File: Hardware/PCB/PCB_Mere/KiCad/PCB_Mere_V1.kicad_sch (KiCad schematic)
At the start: 24 parts, among them U1 STM32H723ZGTx, U2 SX1276

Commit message: Add files via upload
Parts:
- removed U1: STM32H723ZGTx, Package_QFP:LQFP-144_20x20mm_P0.5mm, symbol MCU_ST_STM32H7:STM32H723ZGTx
- removed U2: SX1276, Package_DFN_QFN:QFN-28-1EP_6x6mm_P0.65mm_EP4.8x4.8mm, symbol RF:SX1276
- added U1: STM32H723ZGT6, EasyEDA:LQFP-144_L20.0-W20.0-P0.50-LS22.0-BL, symbol EasyEDA:STM32H723ZGT6
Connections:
- net +3.3V: now also C2.1, U1.107 (VSS), U1.108 (VDD), U1.120 (VSS), U1.121 (VDD), U1.130 (VSS), U1.131 (VDD), U1.143 (PDR_ON), U1.144 (VDD), U1.16 (VSS), U1.17 (VDD), U1.30 (VDD), U1.31 (VSSA), U1.32 (VREF+), U1.33 (VDDA), U1.38 (VSS), U1.39 (VDD), U1.51 (VSS), U1.52 (VDD), U1.6 (VBAT), U1.61 (VSS), U1.62 (VDD), U1.72 (VDD), U1.83 (VSS), U1.84 (VDD), U1.94 (VSS), U1.95 (VDD33USB); no longer C2.2
- net DEBUG_JTCK-SWCLK: now also U1.109 (PA14)
- net DEBUG_JTDO-SWO: now also U1.133 (PB3)
- net DEBUG_JTMS-SWDIO: now also U1.105 (PA13)
- net ESP32_UART7_RX: now also U1.58 (PE7)
- net ESP32_UART7_TX: now also U1.59 (PE8)
- net ETAT-B-ON/OFF_GPIO_Input: now also U1.29 (PC3_C)
- net GNSS_UART5_RX: now also U1.73 (PB12)
- net GNSS_UART5_TX: now also U1.74 (PB13)
- net ID-EXT_ADC1_INP14: now also U1.36 (PA2)
- net IMU-F_I2C2_SCL: now also U1.11 (PF1)
- net IMU-F_I2C2_SDA: now also U1.10 (PF0)
- net IMU-M_I2C1_SCL: now also U1.136 (PB6)
- net IMU-M_I2C1_SDA: now also U1.137 (PB7)
- net JOYSTICK_ADC1_INP10: now also U1.26 (PC0)
- net JOYSTICK_ADC1_INP11: now also U1.27 (PC1)
- net JOYSTICK_GPIO_Input: now also U1.28 (PC2_C)
- net JTAG_UART9_RX: now also U1.56 (PG0)
- net JTAG_UART9_TX: now also U1.57 (PG1)
- net LED1_ETAT_GPIO_Output: now also U1.81 (PD12)
- net LED2_DEBUG_GPIO_Output: now also U1.80 (PD11)
- net LIDAR_UART8_RX: now also U1.141 (PE0)
- net LIDAR_UART8_TX: now also U1.142 (PE1)
- net LoRa_SPI1_MISO: now also U1.124 (PG9)
- net LoRa_SPI1_MOSI: now also U1.123 (PD7)
- net LoRa_SPI1_NSS: now also U1.125 (PG10)
- net LoRa_SPI1_SCK: now also U1.126 (PG11)
- net SCREEN_SPI5_MISO: now also U1.20 (PF8)
- net SCREEN_SPI5_MOSI: now also U1.21 (PF9)
- net SCREEN_SPI5_NSS: now also U1.18 (PF6)
- net SCREEN_SPI5_SCK: now also U1.19 (PF7)
- net SD_CK: now also U1.113 (PC12)
- net SD_CMD: now also U1.116 (PD2)
- net SD_D0: now also U1.98 (PC8)
- net SD_D1: now also U1.99 (PC9)
- net SD_D2: now also U1.111 (PC10)
- net SD_D3: now also U1.112 (PC11)
- net SD_DETECT: now also U1.97 (PC7)
- net STEPPER-AZ_TIM8_CH1: now also U1.96 (PC6)
- net STEPPER-EL_TIM1_CH1: now also U1.60 (PE9)
- net TMC2209_AZ_DIAG_GPIO_Input: now also U1.87 (PG2)
- net TMC2209_AZ_DIR_GPIO_Output: now also U1.90 (PG5)
- net TMC2209_AZ_ENABLE_GPIO_Output: now also U1.92 (PG7)
- net TMC2209_AZ_INDEX_GPIO_Input: now also U1.86 (PD15)
- net TMC2209_AZ_MS1_GPIO_Output: now also U1.89 (PG4)
- net TMC2209_AZ_MS2_GPIO_Output: now also U1.88 (PG3)
- net TMC2209_AZ_STEP_GPIO_Output: now also U1.91 (PG6)
- net TMC2209_AZ_USART1_RX: now also U1.76 (PB15)
- net TMC2209_AZ_USART1_TX: now also U1.75 (PB14)
- net TMC2209_EL_DIAG_GPIO_Input: now also U1.68 (PE15)
- net TMC2209_EL_DIR_GPIO_Output: now also U1.65 (PE12)
- net TMC2209_EL_ENABLE_GPIO_Output: now also U1.63 (PE10)
- net TMC2209_EL_INDEX_GPIO_Input: now also U1.69 (PB10)
- net TMC2209_EL_MS1_GPIO_Output: now also U1.66 (PE13)
- net TMC2209_EL_MS2_GPIO_Output: now also U1.67 (PE14)
- net TMC2209_EL_STEP_GPIO_Output: now also U1.64 (PE11)
- net TMC2209_EL_USART3_RX: now also U1.70 (PB11)
- net TMC2209_EL_USART3_TX: now also U1.77 (PD8)
- net at C7.2: now also U1.25 (NRST)
- net at R1.2: now also U1.138 (BOOT0)
- net at C3.1: now also U1.106 (VCAP)
- new net: C2.2, U1.71 (VCAP)
- new net SCREEN_RST_GPIO_Output: U1.22 (PF10)
- no-connect marks 57 -> 56
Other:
- added sheet Composant_Mère (Composant_Mere.kicad_sch)
- added sheet Connecteurs -> PCB (Connecteurs.kicad_sch)
- note added: "STM32H723ZGTx"
- note removed: "STM32H723ZGTx Main PCB Mère"
- moved on the sheet: C1, C10, C11, C12, C13, C14, C15, C16, C17, C18, C19, C2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

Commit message: push du kicad
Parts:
- removed R1: 10k, symbol Device:R_Small
- added C30: 10n, symbol Device:C_Small
- added R14: 10k, symbol Device:R_Small
- added SW1: NRST_BTN, EasyEDA:KEY-SMD_4P-L3.5-W2.9-P1.48-LS4.3-TL, symbol EasyEDA:EVPAA202K
- added SW2: BOOT_BTN, EasyEDA:KEY-SMD_4P-L3.5-W2.9-P1.48-LS4.3-TL, symbol EasyEDA:EVPAA202K
- C7: value 100n -> 0,1µ
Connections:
- net +3.3V: now also C7.2, C30.1, R14.2, SW1.2, SW2.2'; no longer C7.1
- net ETAT-B-ON/OFF_GPIO_Input: now also U1.45 (PC5)
- net NRST_STM: now reaches U1.25 (NRST)
- net NRST_STM: now also C7.1, SW1.1'; no longer C7.2
- net at U1.138 (BOOT0): now also C30.2, R14.1, SW2.1
- net TACTIL_SPI6_NSS: now reaches U1.40 (PA4)
- net TACTIL_SPI6_SCK: now reaches U1.41 (PA5)
- net TACTIL_SPI6_MISO: now reaches U1.42 (PA6)
- net TACTIL_SPI6_MOSI: now reaches U1.43 (PA7)
- net TACTIL_GPIO_EXTI4: now reaches U1.44 (PC4)
- net BONUS1_GPIO: now reaches U1.46 (PB0)
- net BONUS2_GPIO: now reaches U1.47 (PB1)
- no-connect marks 56 -> 52

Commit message: Dernière version Schématique
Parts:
- C1, C10, C11, C12, C13, C14, C15, C16, C17, C18, C19, C21, C6, C7, C8, C9: footprint (none) -> Capacitor_SMD:C_0201_0603Metric; LCSC Part (none) -> C49062
- C2, C3: footprint (none) -> Capacitor_SMD:C_0201_0603Metric; LCSC Part (none) -> C307418
- C20: footprint (none) -> Capacitor_SMD:C_0201_0603Metric; LCSC Part (none) -> C19702
- C30: footprint (none) -> Capacitor_SMD:C_0402_1005Metric; LCSC Part (none) -> C19702
- C4, C5: footprint (none) -> Capacitor_SMD:C_0201_0603Metric; LCSC Part (none) -> C52923
- R14: footprint (none) -> Resistor_SMD:R_0201_0603Metric; LCSC Part (none) -> C100126
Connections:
- net LED2_DEBUG_GPIO_Output: no longer names the net of U1.80 (PD11)
- no-connect marks 52 -> 53

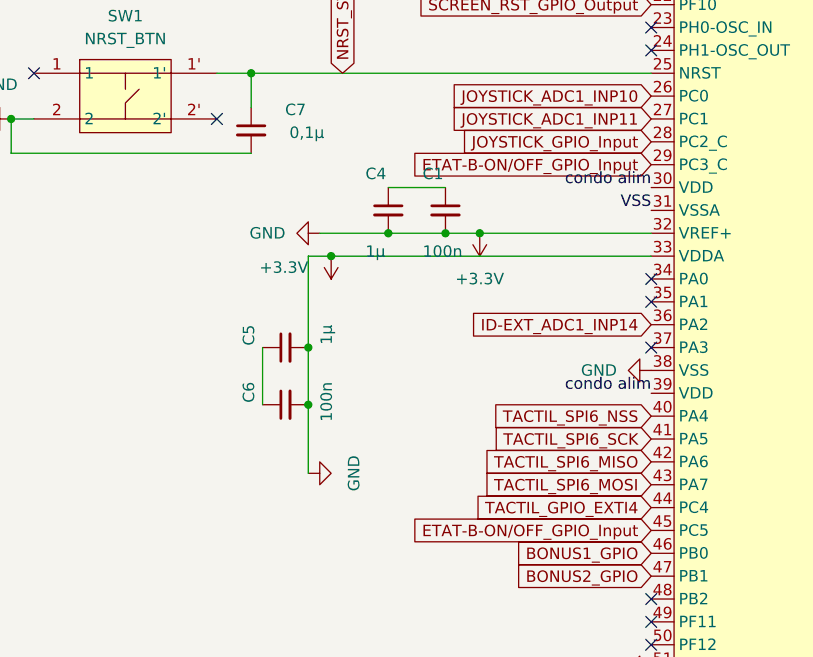
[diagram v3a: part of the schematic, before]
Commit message: Nouvelles empreintes de mounting holes et plusieurs court circuits retirés du schematic
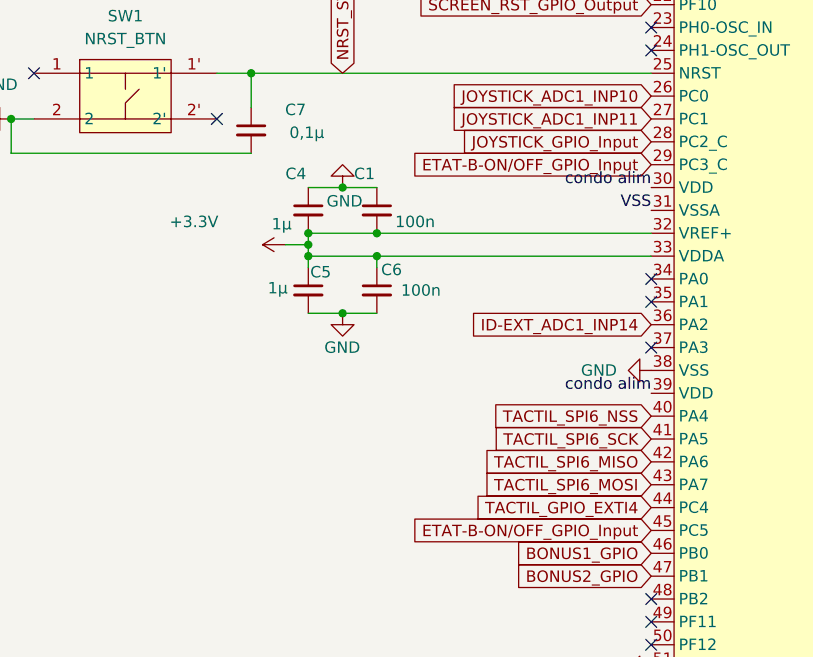
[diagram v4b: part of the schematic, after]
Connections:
- net +3.3V: now also C5.1, C6.1; no longer C10.2, C11.2, C12.2, C13.2, C14.2, C15.2, C16.2, C17.2, C18.2, C19.2, C2.1, C20.2, C21.2, C3.2, C30.1, C5.2, C6.2, C7.2, C8.2, C9.2, R14.2, SW1.2, U1.107 (VSS), U1.120 (VSS), U1.130 (VSS), U1.16 (VSS), U1.31 (VSSA), U1.38 (VSS), U1.51 (VSS), U1.61 (VSS), U1.83 (VSS), U1.94 (VSS)
- net GND: now reaches C1.1, C4.1
- net GND: now also C10.2, C11.2, C12.2, C13.2, C14.2, C15.2, C16.2, C17.2, C18.2, C19.2, C2.1, C20.2, C21.2, C3.2, C30.1, C5.2, C6.2, C7.2, C8.2, C9.2, R14.2, SW1.2, U1.107 (VSS), U1.120 (VSS), U1.130 (VSS), U1.16 (VSS), U1.31 (VSSA), U1.38 (VSS), U1.51 (VSS), U1.61 (VSS), U1.83 (VSS), U1.94 (VSS)
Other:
- moved on the sheet: C1, C4, C5, C6

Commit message: Push PCB_Mère avancement routage
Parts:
- added C40, C41: 22p, Capacitor_SMD:C_0402_1005Metric, symbol Device:C_Small
- added R17, R18: 1k, Resistor_SMD:R_0402_1005Metric, symbol Device:R_Small
- added X1: X322525MOB4SI, EasyEDA:CRYSTAL-SMD_4P-L3.2-W2.5-BL, symbol EasyEDA:X322525MOB4SI
- C1, C10, C11, C12, C13, C14, C15, C16, C17, C18, C19, C20, C21, C4, C5, C6, C7, C8, C9: footprint Capacitor_SMD:C_0201_0603Metric -> Capacitor_SMD:C_0402_1005Metric
- C2, C3: footprint Capacitor_SMD:C_0201_0603Metric -> Capacitor_SMD:C_0603_1608Metric
- R14: footprint Resistor_SMD:R_0201_0603Metric -> Resistor_SMD:R_0402_1005Metric
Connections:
- net ESP32_UART7_RX: now also R18.2; no longer U1.58 (PE7)
- net ESP32_UART7_TX: now also R17.2; no longer U1.59 (PE8)
- net GND: now also C40.2, C41.1, X1.2 (GND), X1.4 (GND)
- net at U1.100 (PA8): now also R18.1
- net at U1.110 (PA15): now also R17.1
- net LoRa_NRST_STM_GPIO_Output: now reaches U1.114 (PD0)
- net OSC_IN: now reaches U1.23 (PH0-OSC_IN)
- net OSC_IN: now also C41.2, X1.1 (OSC1)
- net OSC_OUT: now reaches U1.24 (PH1-OSC_OUT)
- net OSC_OUT: now also C40.1, X1.3 (OSC2)
- net TMC2209_EL_STDBY_GPIO_Output: now reaches U1.78 (PD9)
- net TMC2209_AZ_STDBY_GPIO_Output: now reaches U1.85 (PD14)
- net TMC2209_AZ_STEP_GPIO_Output renamed TMC2209_AZ_SPREAD_GPIO_Output
- net TMC2209_EL_STEP_GPIO_Output renamed TMC2209_EL_SPREAD_GPIO_Output
- no-connect marks 53 -> 48

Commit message: last version
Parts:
- C1, C10, C11, C12, C13, C14, C15, C16, C17, C18, C19, C21, C6, C7, C8, C9: LCSC Part C49062 -> C1525
- C2, C3: LCSC Part C307418 -> C23630
- C20: LCSC Part C19702 -> C77000
- C30: LCSC Part C19702 -> C15195
- C40, C41: LCSC Part C76924 -> C1555
- R14: LCSC Part C100126 -> C25744
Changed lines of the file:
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@@
 			)
 		)
-		(property "LCSC Part" "C49062"
+		(property "LCSC Part" "C1525"
 			(at 104.14 48.26 0)
 			(hide yes)
@@
 			)
 		)
-		(property "LCSC Part" "C19702"
+		(property "LCSC Part" "C77000"
 			(at 38.1 48.26 0)
 			(hide yes)
@@
 			)
 		)
-		(property "LCSC Part" "C49062"
+		(property "LCSC Part" "C1525"
 			(at 73.66 48.26 0)
 			(hide yes)
@@
 			)
 		)
-		(property "LCSC Part" "C49062"
+		(property "LCSC Part" "C1525"
 			(at 53.34 48.26 0)
 			(hide yes)
@@
 			)
 		)
-		(property "LCSC Part" "C76924"
+		(property "LCSC Part" "C1555"
 			(at 30.48 110.49 90)
 			(hide yes)
@@
 			)
 		)
-		(property "LCSC Part" "C307418"
+		(property "LCSC Part" "C23630"
 			(at 146.05 165.1 90)
 			(hide yes)
@@
 			)
 		)
-		(property "LCSC Part" "C49062"
+		(property "LCSC Part" "C1525"
 			(at 48.26 48.26 0)
 			(hide yes)
@@
 			)
 		)
-		(property "LCSC Part" "C49062"
+		(property "LCSC Part" "C1525"
 			(at 83.82 48.26 0)
 			(hide yes)
@@
 			)
 		)
-		(property "LCSC Part" "C49062"
+		(property "LCSC Part" "C1525"
 			(at 53.34 135.89 0)
 			(hide yes)
@@
 			)
 		)
-		(property "LCSC Part" "C49062"
+		(property "LCSC Part" "C1525"
 			(at 43.18 48.26 0)
 			(hide yes)
@@
 			)
 		)
-		(property "LCSC Part" "C49062"
+		(property "LCSC Part" "C1525"
 			(at 58.42 48.26 0)
 			(hide yes)
@@
 			)
 		)
-		(property "LCSC Part" "C49062"
+		(property "LCSC Part" "C1525"
 			(at 67.31 153.67 0)
 			(hide yes)
@@
 			)
 		)
-		(property "LCSC Part" "C49062"
+		(property "LCSC Part" "C1525"
 			(at 67.31 144.78 0)
 			(hide yes)
@@
 			)
 		)
-		(property "LCSC Part" "C49062"
+		(property "LCSC Part" "C1525"
 			(at 68.58 48.26 0)
 			(hide yes)
@@
 			)
 		)
-		(property "LCSC Part" "C49062"
+		(property "LCSC Part" "C1525"
 			(at 99.06 48.26 0)
 			(hide yes)
@@
 			)
 		)
-		(property "LCSC Part" "C100126"
+		(property "LCSC Part" "C25744"
 			(at 182.88 86.36 90)
 			(hide yes)
@@
 			)
 		)
-		(property "LCSC Part" "C76924"
+		(property "LCSC Part" "C1555"
 			(at 53.34 110.49 90)
 			(hide yes)
@@
 			)
 		)
-		(property "LCSC Part" "C307418"
+		(property "LCSC Part" "C23630"
 			(at 95.25 246.38 90)
 			(hide yes)
@@
 			)
 		)
-		(property "LCSC Part" "C19702"
+		(property "LCSC Part" "C15195"
 			(at 176.53 86.36 0)
 			(hide yes)
@@
 			)
 		)
-		(property "LCSC Part" "C49062"
+		(property "LCSC Part" "C1525"
 			(at 88.9 48.26 0)
 			(hide yes)
@@
 			)
 		)
-		(property "LCSC Part" "C49062"
+		(property "LCSC Part" "C1525"
 			(at 63.5 48.26 0)
 			(hide yes)
@@
 			)
 		)
-		(property "LCSC Part" "C49062"
+		(property "LCSC Part" "C1525"
 			(at 78.74 48.26 0)
 			(hide yes)
@@
 			)
 		)
-		(property "LCSC Part" "C49062"
+		(property "LCSC Part" "C1525"
 			(at 93.98 48.26 0)
 			(hide yes)

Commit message: last version
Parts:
- BOOT_BTN-2: renamed from SW2; value BOOT_BTN -> switch
- C7: value 0,1µ -> 100n
- NRST_BTN-1: renamed from SW1; value NRST_BTN -> switch
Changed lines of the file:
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@@
 			)
 		)
-		(property "Value" "0,1µ"
+		(property "Value" "100n"
 			(at 61.468 136.144 0)
 			(show_name no)
@@
 		(dnp no)
 		(fields_autoplaced yes)
-		(property "Reference" "SW2"
+		(property "Reference" "BOOT_BTN-2"
 			(at 175.26 66.0399 90)
 			(show_name no)
@@
 			)
 		)
-		(property "Value" "BOOT_BTN"
+		(property "Value" "switch"
 			(at 175.26 68.5799 90)
 			(show_name no)
@@
 			(project "PCB_Mere_V1"
 				(path "/d2ac468b-9b53-4c3c-b006-996db3620a48"
-					(reference "SW2")
+					(reference "BOOT_BTN-2")
 					(unit 1)
 				)
@@
 		(dnp no)
 		(fields_autoplaced yes)
-		(property "Reference" "SW1"
+		(property "Reference" "NRST_BTN-1"
 			(at 39.37 123.19 0)
 			(show_name no)
@@
 			)
 		)
-		(property "Value" "NRST_BTN"
+		(property "Value" "switch"
 			(at 39.37 125.73 0)
 			(show_name no)
@@
 			(project "PCB_Mere_V1"
 				(path "/d2ac468b-9b53-4c3c-b006-996db3620a48"
-					(reference "SW1")
-					(unit 1)
-				)
+					(reference "NRST_BTN-1")
+					(unit 1)
+				)

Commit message: last version
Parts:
- R17, R18: LCSC Part C102683 -> C11702
- SW1: renamed from NRST_BTN-1; value switch -> (none)
- SW2: renamed from BOOT_BTN-2; value switch -> (none)
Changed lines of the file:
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@@
 			)
 		)
-		(property "LCSC Part" "C102683"
+		(property "LCSC Part" "C11702"
 			(at 153.67 154.94 90)
 			(hide yes)
@@
 		(dnp no)
 		(fields_autoplaced yes)
-		(property "Reference" "BOOT_BTN-2"
+		(property "Reference" "SW2"
 			(at 175.26 66.0399 90)
 			(show_name no)
@@
 			)
 		)
-		(property "Value" "switch"
+		(property "Value" ""
 			(at 175.26 68.5799 90)
 			(show_name no)
@@
 			(project "PCB_Mere_V1"
 				(path "/d2ac468b-9b53-4c3c-b006-996db3620a48"
-					(reference "BOOT_BTN-2")
+					(reference "SW2")
 					(unit 1)
 				)
@@
 		(dnp no)
 		(fields_autoplaced yes)
-		(property "Reference" "NRST_BTN-1"
+		(property "Reference" "SW1"
 			(at 39.37 123.19 0)
 			(show_name no)
@@
 			)
 		)
-		(property "Value" "switch"
+		(property "Value" ""
 			(at 39.37 125.73 0)
 			(show_name no)
@@
 			(project "PCB_Mere_V1"
 				(path "/d2ac468b-9b53-4c3c-b006-996db3620a48"
-					(reference "NRST_BTN-1")
+					(reference "SW1")
 					(unit 1)
 				)
@@
 			)
 		)
-		(property "LCSC Part" "C102683"
+		(property "LCSC Part" "C11702"
 			(at 149.86 180.34 90)
 			(hide yes)
